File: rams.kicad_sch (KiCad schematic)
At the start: 8 parts, among them U12 SIM4X32, U13 SIM4X32, U14 SIM4X32, U15 SIM4X32, U16 SIM4X32, U17 SIM4X32, U18 SIM4X32, U19 SIM4X32

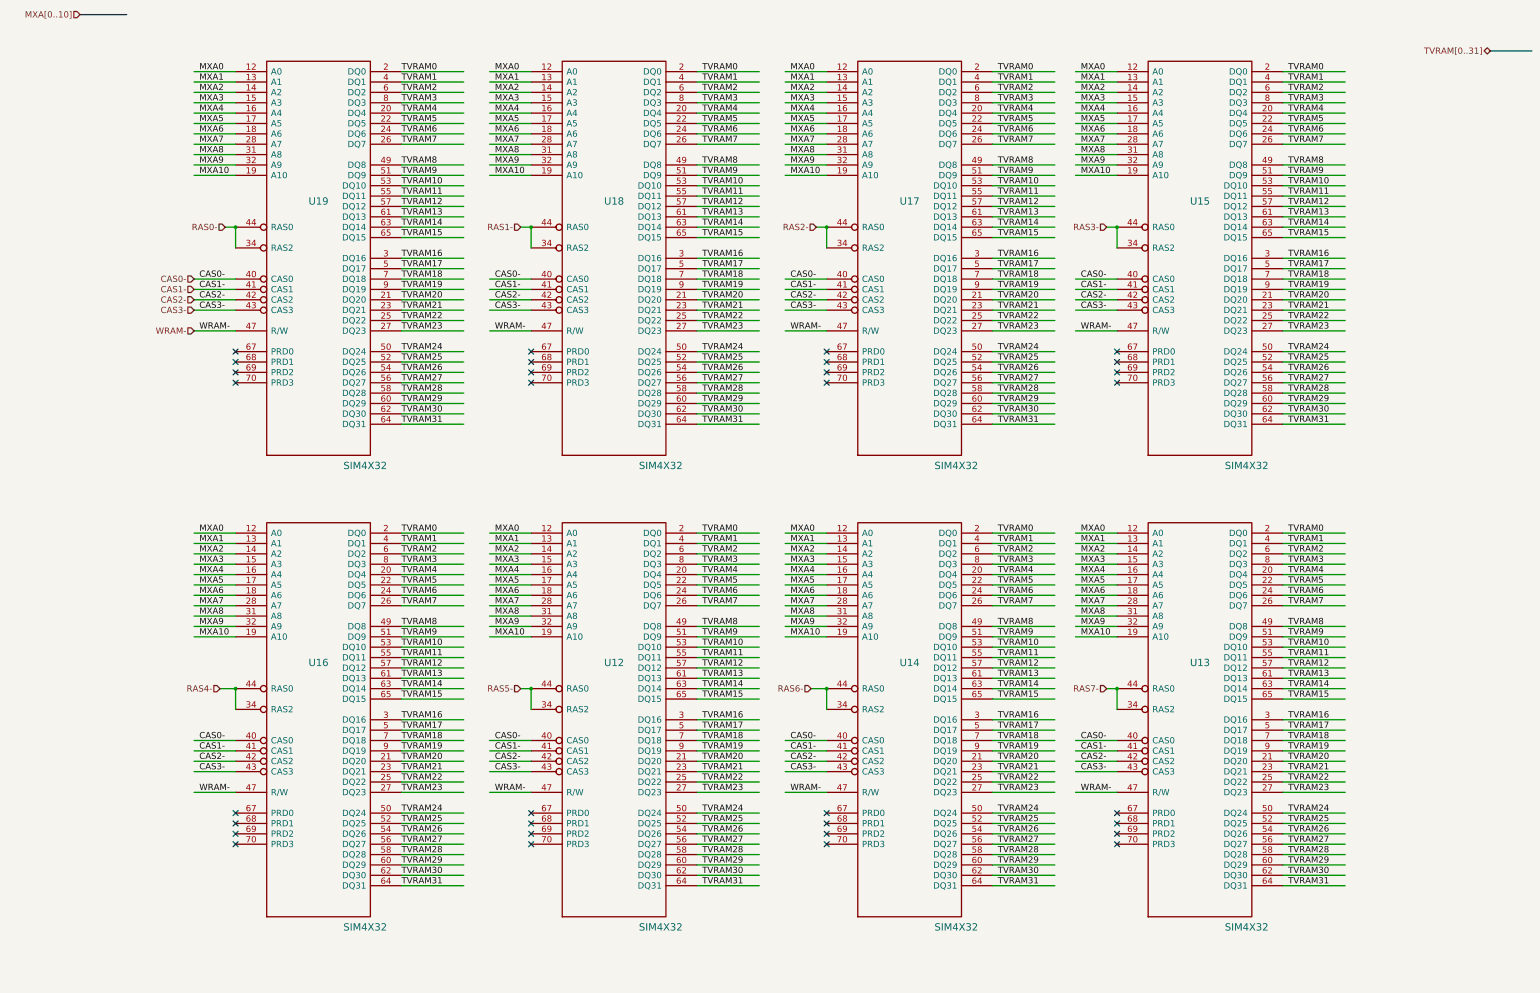
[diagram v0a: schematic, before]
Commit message: update to kicad 9
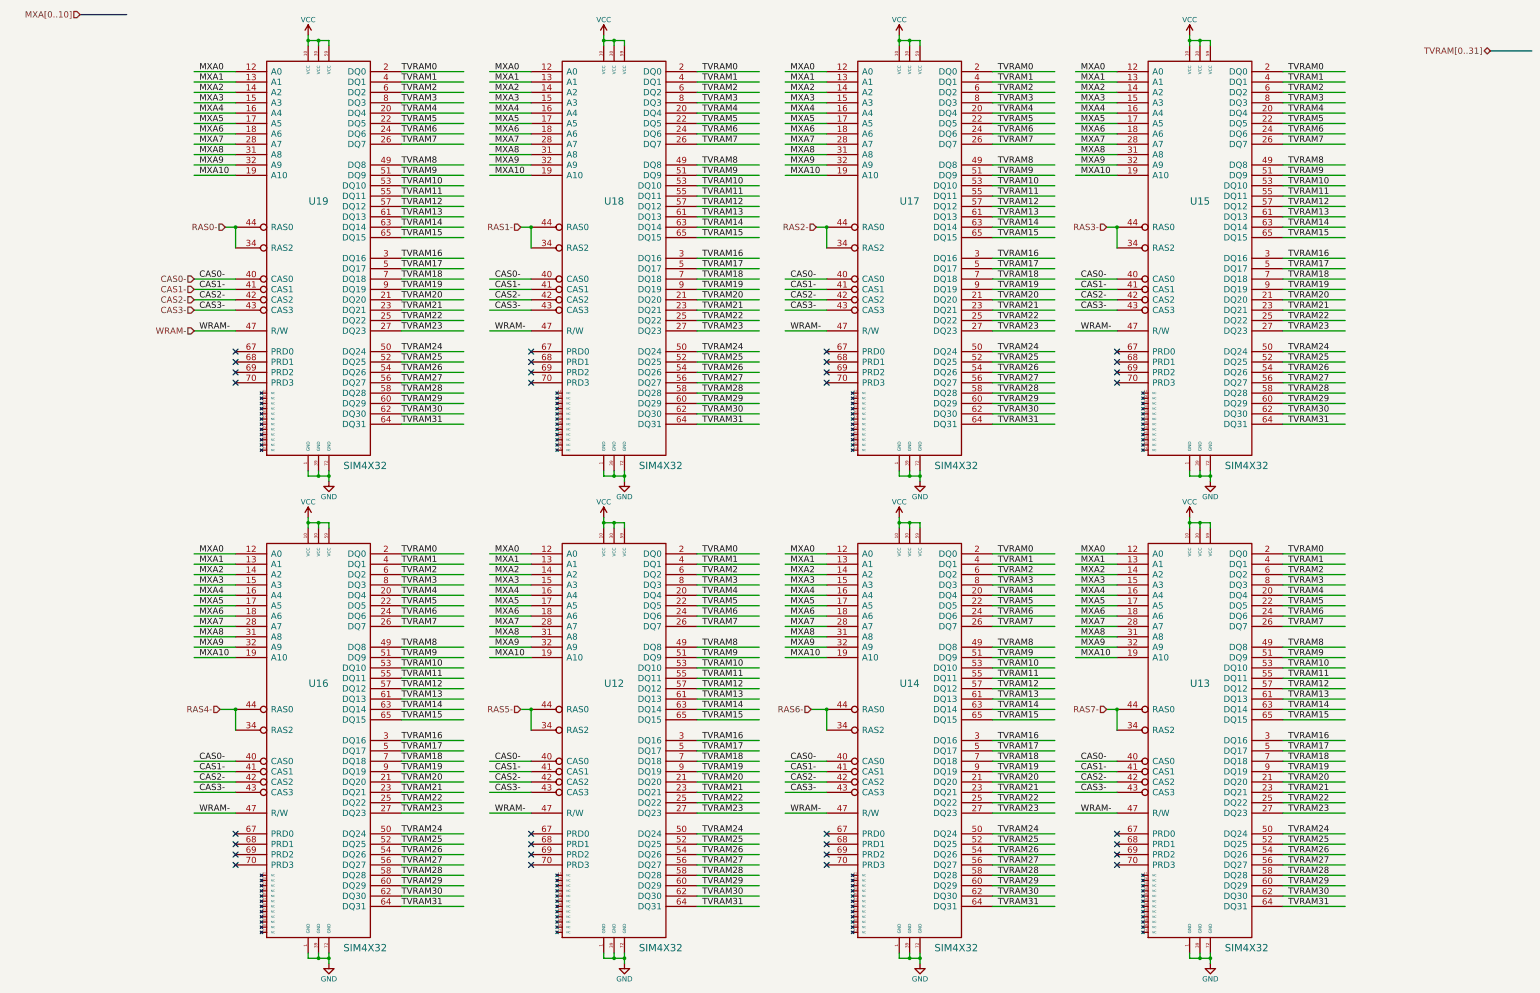
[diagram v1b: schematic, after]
